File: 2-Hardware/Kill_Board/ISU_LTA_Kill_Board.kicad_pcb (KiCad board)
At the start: 2 copper layers, 157.5 x 36.2 mm, 30 parts, among them P1 CONN_01X02, P10 CONN_2, P11 CONN_2, P12 CONN_2, P2 CONN_01X02, P3 CONN_01X02, P4 CONN_01X03, P5 CONN_01X03, P6 CONN_01X03, P7 CONN_2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

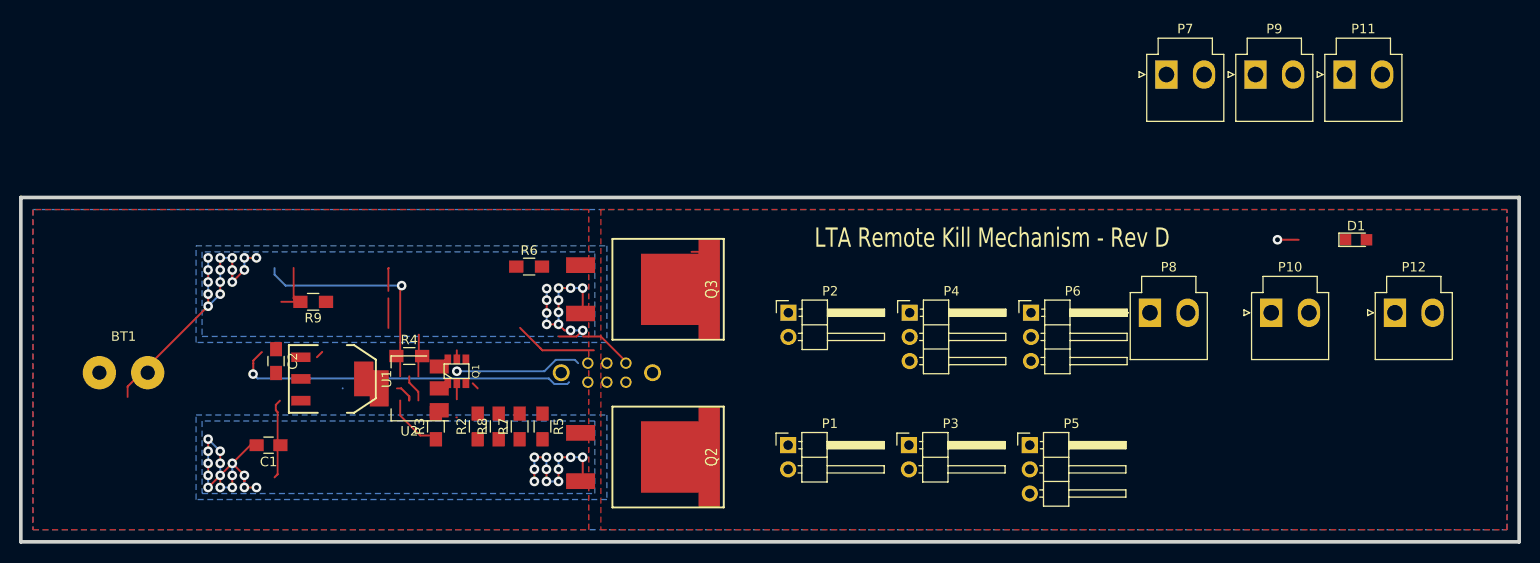
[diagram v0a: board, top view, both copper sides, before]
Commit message: Got correct footprint for feather, placed all parts on board
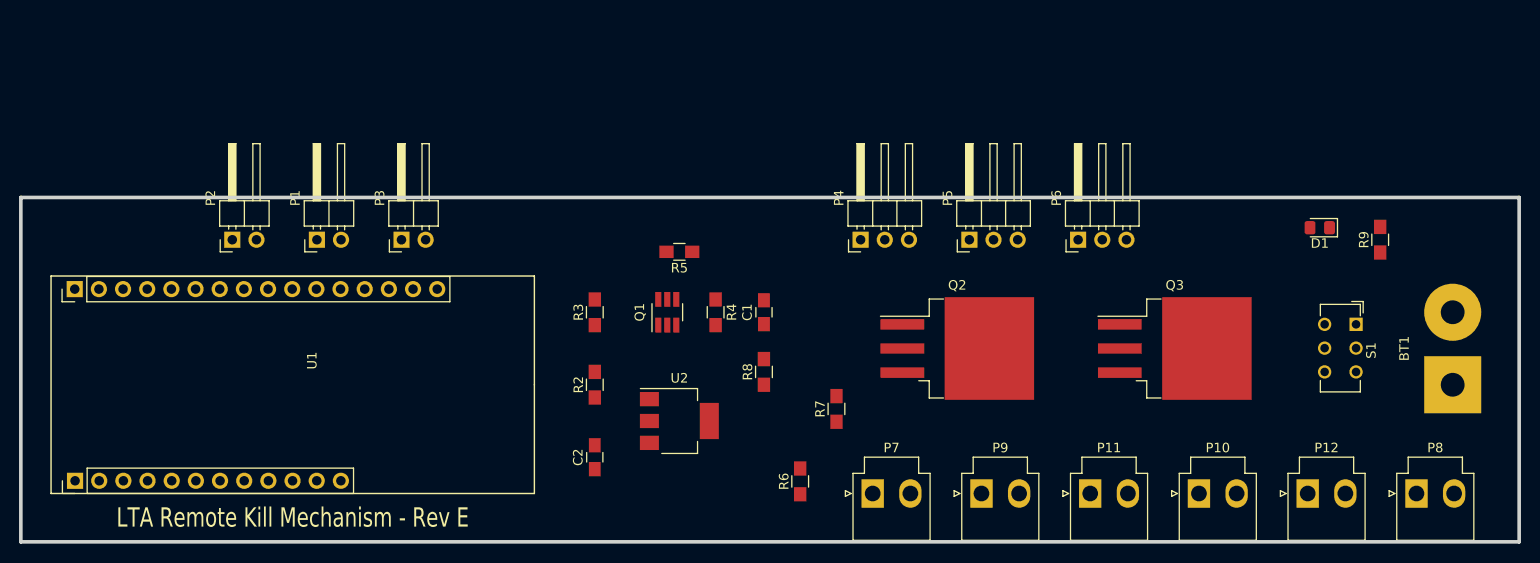
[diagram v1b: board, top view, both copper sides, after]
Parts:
- BT1: footprint Wire_Pads:SolderWirePad_2x_1-5mmDrill -> Connector_Wire:SolderWirePad_1x02_P7.62mm_Drill2.5mm
- D1: footprint LEDs:LED_0805 -> LED_SMD:LED_0805_2012Metric_Pad1.15x1.40mm_HandSolder
- Q1: footprint SOT23_6 -> Package_TO_SOT_SMD:SOT-23-6_Handsoldering
- Q2, Q3: footprint D2PACK -> Package_TO_SOT_SMD:TO-263-3_TabPin2
- S1: footprint DPDT_ESWITCH -> Button_Switch_THT:SW_CuK_JS202011CQN_DPDT_Straight
- U1: footprint SOT223 -> Adafruit:AdafruitFeather
- U2: footprint TO_SOT_Packages_SMD:SOT-223 -> Package_TO_SOT_SMD:SOT-223
- moved BT1 139.7 mm to (179.1, 83.8), turned to 90 degrees
- moved R9 112.3 mm to (171.4, 68.6), turned to 90 degrees
- moved S1 78.9 mm to (168.9, 77.5), turned to 270 degrees
- moved Q3 59.4 mm to (149.9, 80.0), turned to 0 degrees
- moved P2 59.0 mm to (50.8, 68.6), turned to 90 degrees
- moved P3 57.5 mm to (68.6, 68.6), turned to 90 degrees
- moved P1 54.0 mm to (59.7, 68.6), turned to 90 degrees
- moved C1 53.9 mm to (106.7, 76.2), turned to 90 degrees
- moved P7 53.8 mm to (118.1, 95.2)
- moved P9 52.6 mm to (129.5, 95.2)
- moved P11 51.5 mm to (141.0, 95.2)
- moved Q2 38.0 mm to (127.0, 80.0), turned to 0 degrees
- moved R6 36.4 mm to (110.5, 94.0), turned to 90 degrees
- moved C2 35.0 mm to (88.9, 91.4), turned to 90 degrees
- moved P8 33.8 mm to (175.3, 95.2)
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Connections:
- P1 pad 1: (no net) -> Net-(P1-Pad1)
- P1 pad 2: (no net) -> Net-(P1-Pad2)
- P2 pad 1: (no net) -> Net-(P2-Pad1)
- P3 pad 1: (no net) -> Net-(P3-Pad1)
- P5 pad 3: (no net) -> Net-(P5-Pad3)
- P6 pad 3: (no net) -> Net-(P6-Pad3)
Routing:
- net GND: track 104.4 -> 0.00 mm, vias 53 -> 0
- net N-0000024: track 37.3 -> 0.00 mm, vias 1 -> 0
- net /Ctrl: track 24.1 -> 0.00 mm, vias 1 -> 0
- net Net-(C1-Pad1): track 14.1 -> 0.00 mm
- net N-0000033: track 13.4 -> 0.00 mm, vias 1 -> 0
- net N-0000032: track 8.73 -> 0.00 mm
- net /V_Sense: track 6.20 -> 0.00 mm
- net Net-(D1-Pad1): track 6.09 -> 0.00 mm
- net Net-(Q1-Pad3): track 4.40 -> 0.00 mm
- net N-0000018: track 2.42 -> 0.00 mm
- net +BATT: track 2.27 -> 0.00 mm, vias 1 -> 0
- net Net-(Q1-Pad2): track 1.68 -> 0.00 mm
- net /High_Side: track 1.27 -> 0.00 mm
- net N-000007: track 0.75 -> 0.00 mm
- removed copper zone on B.Cu, net +BATT
- removed copper zone on F.Cu, net /High_Side
- removed copper zone on B.Cu, net GND
- removed copper zone on F.Cu, net GND
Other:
- board text added: "LTA Remote Kill Mechanism - Rev E"
- board text removed: "LTA Remote Kill Mechanism - Rev D"

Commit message: Update to board
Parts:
- moved R9 5.39 mm to (167.6, 72.4), turned to 180 degrees
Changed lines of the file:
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@@
   )
   (module Resistors_SMD:R_0805_HandSoldering (layer Front)
-    (at 171.45 68.58 90)
+    (at 167.64 72.39 180)
     (descr "Resistor SMD 0805, hand soldering")
     (tags "resistor 0805")
     (attr smd)
-    (fp_text reference R9 (at 0 -1.7 90) (layer F.SilkS)
+    (fp_text reference R9 (at 0 -1.7 180) (layer F.SilkS)
       (effects (font (size 1 1) (thickness 0.15)))
     )
-    (fp_text value 330 (at 0 1.75 90) (layer F.Fab)
+    (fp_text value 330 (at 0 1.75 180) (layer F.Fab)
       (effects (font (size 1 1) (thickness 0.15)))
     )
@@
     (fp_line (start 1 0.62) (end -1 0.62) (layer F.Fab) (width 0.1))
     (fp_line (start -1 0.62) (end -1 -0.62) (layer F.Fab) (width 0.1))
-    (fp_text user %R (at 0 0 90) (layer F.Fab)
+    (fp_text user %R (at 0 0 180) (layer F.Fab)
       (effects (font (size 0.5 0.5) (thickness 0.075)))
     )
-    (pad 2 smd rect (at 1.35 0 90) (size 1.5 1.3) (layers Front F.Paste F.Mask)
+    (pad 2 smd rect (at 1.35 0 180) (size 1.5 1.3) (layers Front F.Paste F.Mask)
       (net 8 "Net-(D1-Pad1)"))
-    (pad 1 smd rect (at -1.35 0 90) (size 1.5 1.3) (layers Front F.Paste F.Mask)
+    (pad 1 smd rect (at -1.35 0 180) (size 1.5 1.3) (layers Front F.Paste F.Mask)
       (net 2 +BATT))
     (model ${KISYS3DMOD}/Resistors_SMD.3dshapes/R_0805.wrl

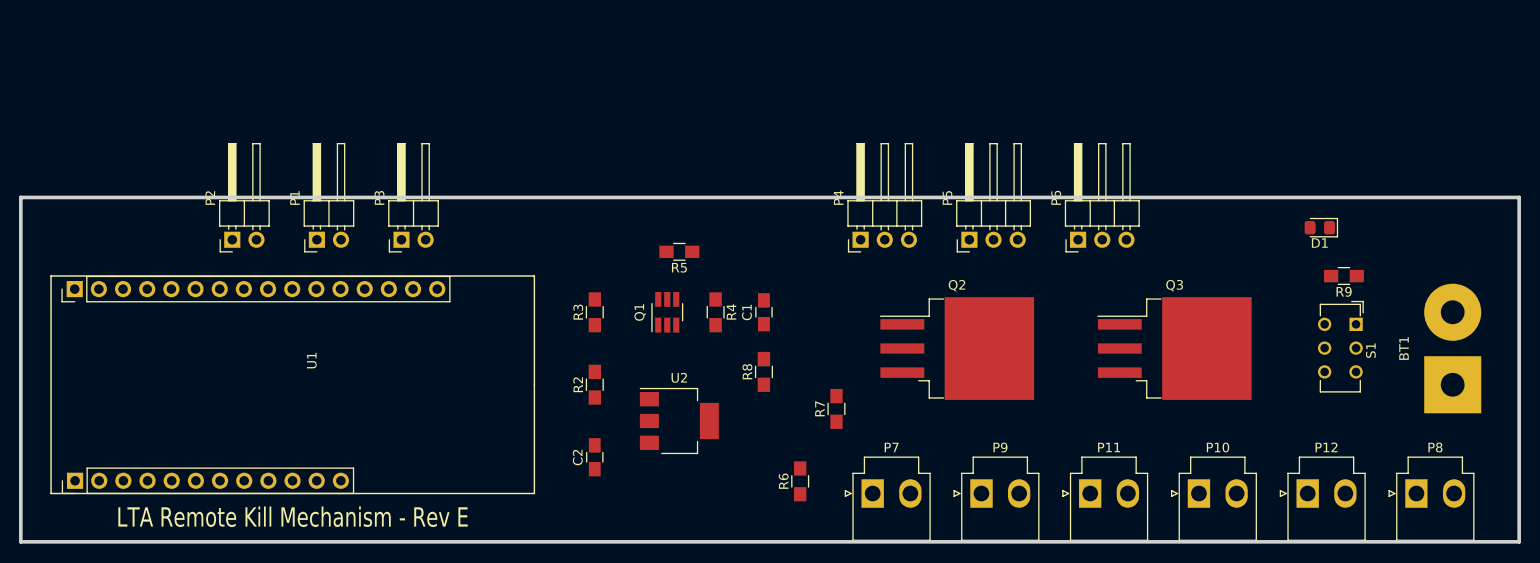
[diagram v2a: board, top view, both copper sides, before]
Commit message: Adding pours
Not done just moving to a new computer.
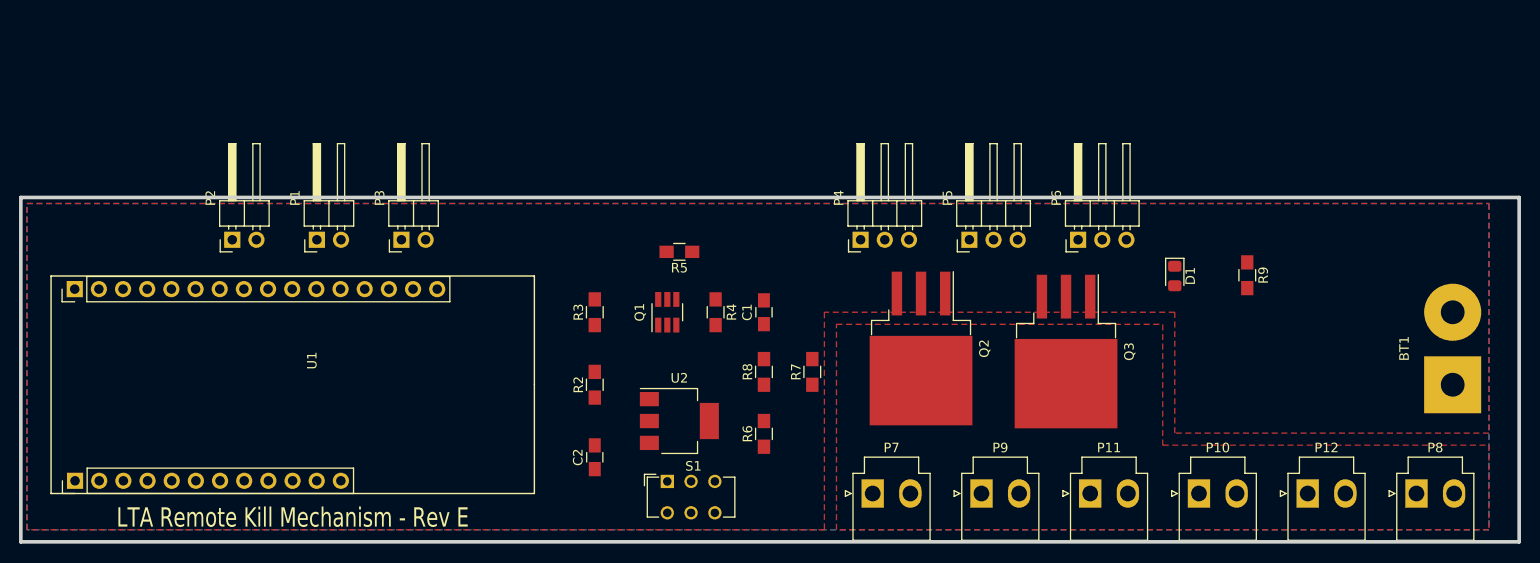
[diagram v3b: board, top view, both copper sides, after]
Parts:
- moved S1 74.2 mm to (96.5, 94.0), turned to 0 degrees
- moved D1 16.1 mm to (149.9, 72.4), turned to 270 degrees
- moved Q3 11.4 mm to (138.4, 80.3), turned to 270 degrees
- moved R9 10.2 mm to (157.5, 72.3), turned to 270 degrees
- moved R6 6.29 mm to (106.7, 89.0)
- moved R7 4.65 mm to (111.8, 82.5)
- moved Q2 3.81 mm to (123.2, 80.0), turned to 270 degrees
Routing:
- added copper zone on B.Cu, net +BATT
- added copper zone on F.Cu, net /High_Side
- added copper zone on F.Cu, net GND

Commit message: Fixed pwm to have 3.3 v power and then added traces.
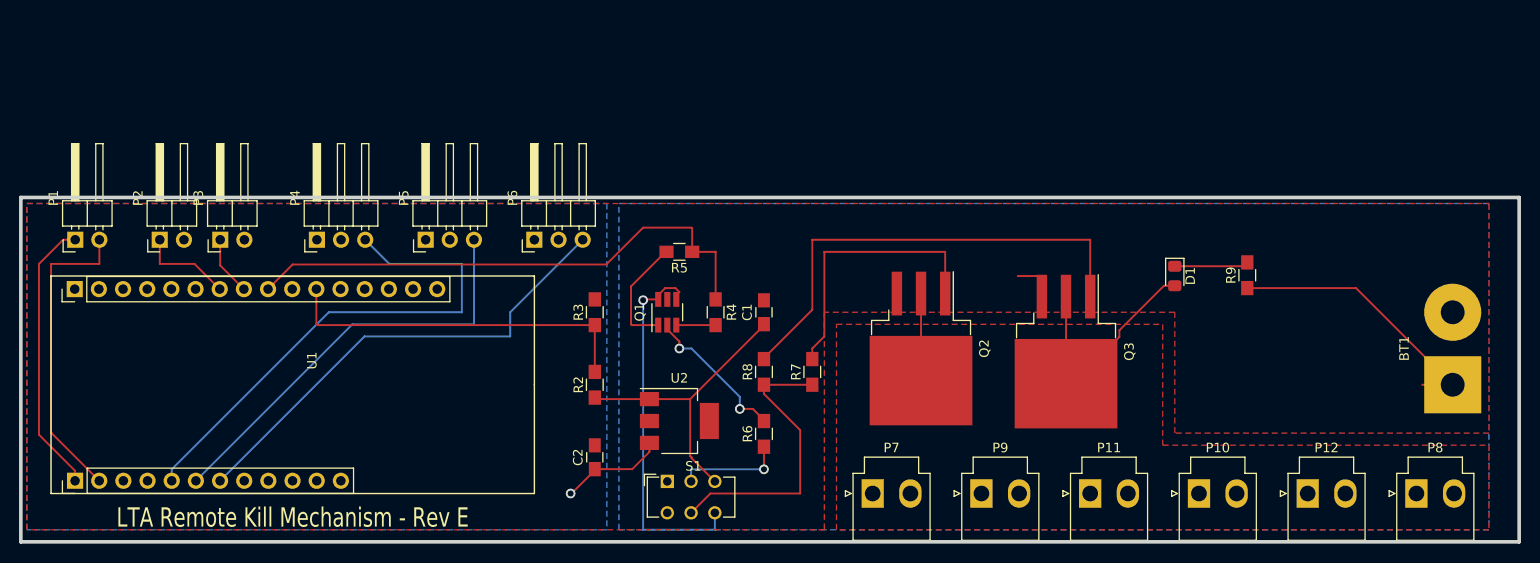
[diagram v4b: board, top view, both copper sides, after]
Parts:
- moved P4 57.2 mm to (59.7, 68.6)
- moved P5 57.2 mm to (71.1, 68.6)
- moved P6 57.1 mm to (82.5, 68.6)
- moved P1 25.4 mm to (34.3, 68.6)
- moved P3 19.0 mm to (49.5, 68.6)
- moved P2 7.62 mm to (43.2, 68.6)
- turned R9 to 90 degrees
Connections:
- P4 pad 2: +BATT -> +3.3V
- P5 pad 2: +BATT -> +3.3V
- P6 pad 2: +BATT -> +3.3V
- S1 pad 1: (no net) -> Net-(S1-Pad1)
- U1 pad 1: (no net) -> Net-(U1-Pad1)
- U1 pad 10: Net-(P6-Pad3) -> Net-(U1-Pad10)
- U1 pad 12: (no net) -> Net-(U1-Pad12)
- U1 pad 14: (no net) -> Net-(U1-Pad14)
- U1 pad 16: (no net) -> Net-(U1-Pad16)
- U1 pad 17: (no net) -> Net-(U1-Pad17)
- U1 pad 18: (no net) -> Net-(U1-Pad18)
- U1 pad 19: (no net) -> Net-(U1-Pad19)
- U1 pad 2: (no net) -> Net-(U1-Pad2)
- U1 pad 20: (no net) -> Net-(U1-Pad20)
- U1 pad 21: (no net) -> Net-(U1-Pad21)
- U1 pad 22: (no net) -> Net-(P6-Pad3)
- U1 pad 23: (no net) -> Net-(P5-Pad3)
- U1 pad 24: (no net) -> Net-(P4-Pad3)
- U1 pad 25: (no net) -> Net-(U1-Pad25)
- U1 pad 26: (no net) -> Net-(U1-Pad26)
- U1 pad 3: (no net) -> Net-(U1-Pad3)
- U1 pad 4: Net-(P4-Pad3) -> Net-(U1-Pad4)
- U1 pad 5: Net-(P5-Pad3) -> Net-(U1-Pad5)
- U1 pad 6: (no net) -> Net-(U1-Pad6)
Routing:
- net /Ctrl: track 0.00 -> 57.2 mm
- net Net-(P4-Pad3): track 0.00 -> 54.8 mm
- net Net-(P6-Pad3): track 0.00 -> 50.1 mm
- net Net-(Q3-Pad1): track 0.00 -> 49.8 mm
- net Net-(P5-Pad3): track 0.00 -> 44.9 mm
- net +BATT: track 0.00 -> 40.3 mm, vias 0 -> 1
- net Net-(Q1-Pad4): track 0.00 -> 39.2 mm, vias 0 -> 1
- net /V_Sense: track 0.00 -> 37.9 mm
- net /High_Side: track 0.00 -> 34.4 mm
- net Net-(P1-Pad2): track 0.00 -> 32.5 mm
- net Net-(C1-Pad1): track 0.00 -> 30.9 mm
- net Net-(R7-Pad1): track 0.00 -> 30.4 mm
- net Net-(P1-Pad1): track 0.00 -> 29.2 mm
- net Net-(Q2-Pad1): track 0.00 -> 28.9 mm
- net Net-(Q1-Pad2): track 0.00 -> 15.8 mm, vias 0 -> 2
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- added copper zone on B.Cu, net +3.3V

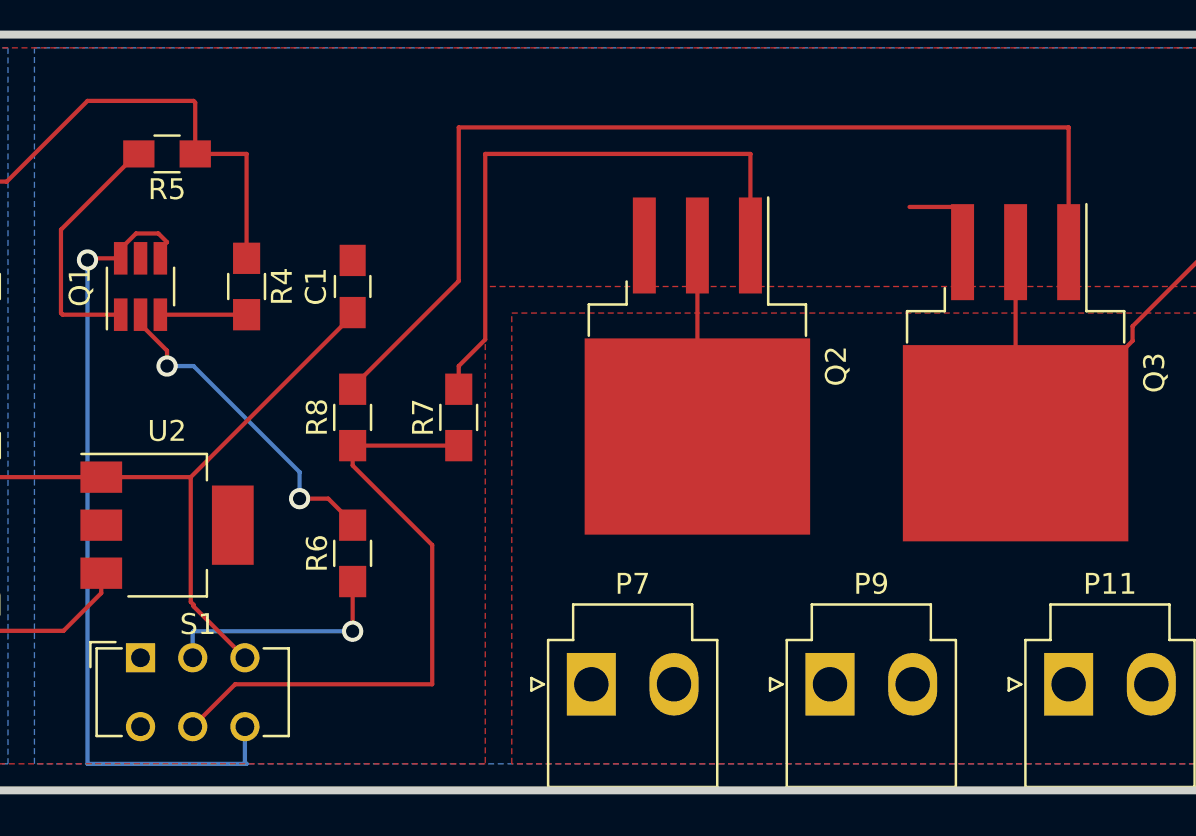
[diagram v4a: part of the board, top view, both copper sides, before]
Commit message: Reduced through holes and fixed the ground issue on one mos
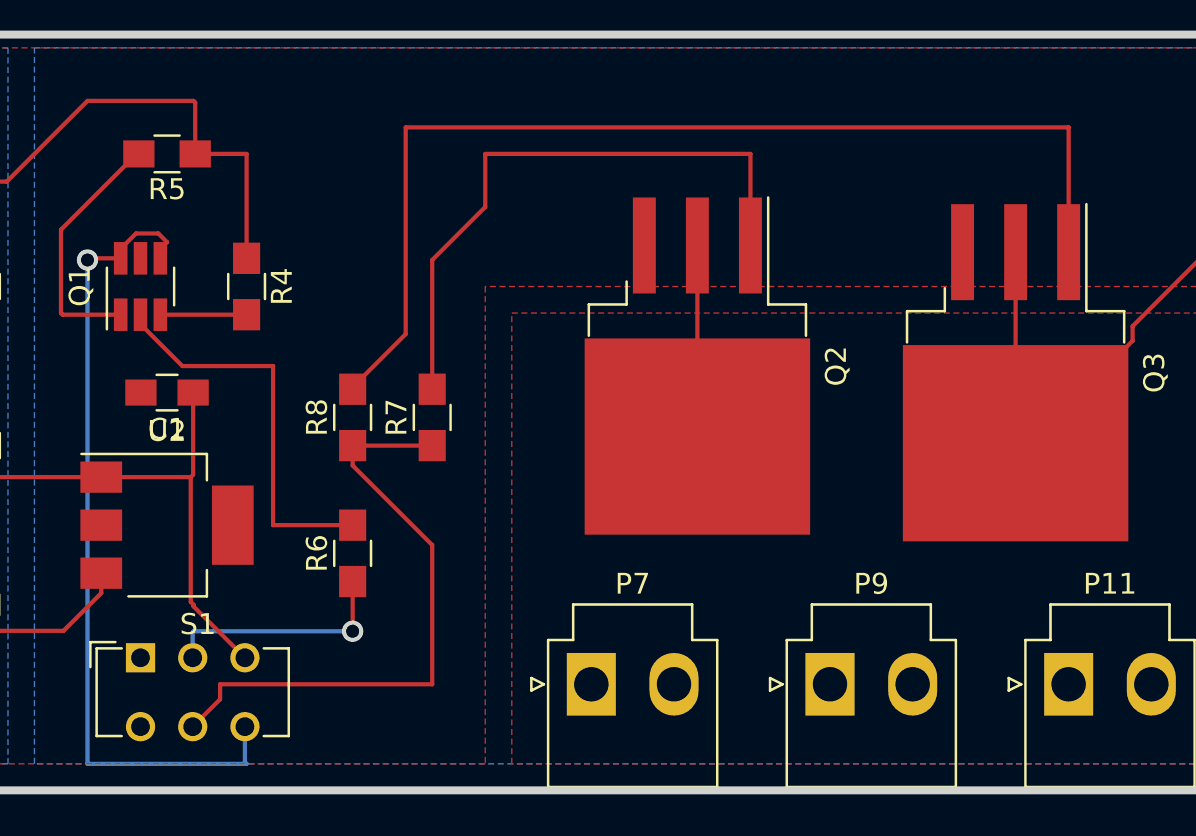
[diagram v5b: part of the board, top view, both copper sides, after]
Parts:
- moved C1 10.2 mm to (97.8, 81.3), turned to 180 degrees
- moved R7 1.27 mm to (110.5, 82.5)
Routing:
- net Net-(C1-Pad1): track 30.9 -> 23.9 mm
- net GND: track 4.46 -> 0.00 mm
- net Net-(Q1-Pad2): track 15.8 -> 19.2 mm, vias 2 -> 0
- net Net-(Q3-Pad1): track 49.8 -> 51.3 mm
- net Net-(R7-Pad1): track 30.4 -> 29.6 mm
- net Net-(Q2-Pad1): track 28.9 -> 29.4 mm
